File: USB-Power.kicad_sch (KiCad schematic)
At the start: 39 parts, among them J3 USB_C_Receptacle_USB2.0_16P, J4 USB_C_Receptacle_USB2.0_16P, SW3 SW_SPDT, U4 USBLC6-2SC6, U5 BQ24075RGT, U6 BQ27441DRZR-G1A, U7 TPS61023DRLT

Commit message: layouting component to PCB
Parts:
- C45, C47, C48, C49, C50, C51, C52, C53: footprint (none) -> Capacitor_SMD:C_0603_1608Metric
- C46, C54: footprint (none) -> Capacitor_SMD:C_0402_1005Metric
- D3, D4: footprint (none) -> LED_SMD:LED_0805_2012Metric
- J3, J4: footprint (none) -> Connector_USB:USB_C_Receptacle_G-Switch_GT-USB-7010ASV
- L3: footprint (none) -> Inductor_SMD:L_Abracon_ASPI-0425
- R11, R12, R13, R14, R15, R16, R17, R18, R19, R20, R21, R22, R23, R24, R25, R26, R27, R28, R29: footprint (none) -> Resistor_SMD:R_0402_1005Metric
- SW3: footprint (none) -> Button_Switch_SMD:SW_SPDT_CK_JS102011SAQN
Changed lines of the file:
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@@
 			)
 		)
-		(property "Footprint" ""
+		(property "Footprint" "Capacitor_SMD:C_0603_1608Metric"
 			(at 272.7452 34.29 0)
 			(effects
@@
 			)
 		)
-		(property "Footprint" ""
+		(property "Footprint" "Connector_USB:USB_C_Receptacle_G-Switch_GT-USB-7010ASV"
 			(at 34.29 104.14 0)
 			(effects
@@
 			)
 		)
-		(property "Footprint" ""
+		(property "Footprint" "Capacitor_SMD:C_0603_1608Metric"
 			(at 147.0152 184.15 0)
 			(effects
@@
 			)
 		)
-		(property "Footprint" ""
+		(property "Footprint" "Resistor_SMD:R_0402_1005Metric"
 			(at 191.262 60.96 90)
 			(effects
@@
 			)
 		)
-		(property "Footprint" ""
+		(property "Footprint" "LED_SMD:LED_0805_2012Metric"
 			(at 251.46 52.07 0)
 			(effects
@@
 			)
 		)
-		(property "Footprint" ""
+		(property "Footprint" "Resistor_SMD:R_0402_1005Metric"
 			(at 74.422 175.26 90)
 			(effects
@@
 			)
 		)
-		(property "Footprint" ""
+		(property "Footprint" "Resistor_SMD:R_0402_1005Metric"
 			(at 55.88 96.52 0)
 			(effects
@@
 			)
 		)
-		(property "Footprint" ""
+		(property "Footprint" "Button_Switch_SMD:SW_SPDT_CK_JS102011SAQN"
 			(at 157.48 34.29 0)
 			(effects
@@
 			)
 		)
-		(property "Footprint" ""
+		(property "Footprint" "Resistor_SMD:R_0402_1005Metric"
 			(at 55.88 30.48 0)
 			(effects
@@
 			)
 		)
-		(property "Footprint" ""
+		(property "Footprint" "Resistor_SMD:R_0402_1005Metric"
 			(at 209.55 128.27 0)
 			(effects
@@
 			)
 		)
-		(property "Footprint" ""
+		(property "Footprint" "Capacitor_SMD:C_0603_1608Metric"
 			(at 65.7352 184.15 0)
 			(effects
@@
 			)
 		)
-		(property "Footprint" ""
+		(property "Footprint" "Resistor_SMD:R_0402_1005Metric"
 			(at 180.34 39.37 0)
 			(effects
@@
 			)
 		)
-		(property "Footprint" ""
+		(property "Footprint" "Resistor_SMD:R_0402_1005Metric"
 			(at 74.422 160.02 90)
 			(effects
@@
 			)
 		)
-		(property "Footprint" ""
+		(property "Footprint" "LED_SMD:LED_0805_2012Metric"
 			(at 251.46 63.5 0)
 			(effects
@@
 			)
 		)
-		(property "Footprint" ""
+		(property "Footprint" "Resistor_SMD:R_0402_1005Metric"
 			(at 55.88 93.98 0)
 			(effects
@@
 			)
 		)
-		(property "Footprint" ""
+		(property "Footprint" "Resistor_SMD:R_0402_1005Metric"
 			(at 151.638 25.4 90)
 			(effects
@@
 			)
 		)
-		(property "Footprint" ""
+		(property "Footprint" "Capacitor_SMD:C_0402_1005Metric"
 			(at 38.1 180.34 0)
 			(effects
@@
 			)
 		)
-		(property "Footprint" ""
+		(property "Footprint" "Capacitor_SMD:C_0603_1608Metric"
 			(at 261.3152 34.29 0)
 			(effects
@@
 			)
 		)
-		(property "Footprint" ""
+		(property "Footprint" "Resistor_SMD:R_0402_1005Metric"
 			(at 266.7 144.78 0)
 			(effects
@@
 			)
 		)
-		(property "Footprint" ""
+		(property "Footprint" "Capacitor_SMD:C_0603_1608Metric"
 			(at 236.22 117.1448 0)
 			(effects
@@
 			)
 		)
-		(property "Footprint" ""
+		(property "Footprint" "Resistor_SMD:R_0402_1005Metric"
 			(at 235.712 36.83 90)
 			(effects
@@
 			)
 		)
-		(property "Footprint" ""
+		(property "Footprint" "Inductor_SMD:L_Abracon_ASPI-0425"
 			(at 93.98 175.26 0)
 			(effects
@@
 			)
 		)
-		(property "Footprint" ""
+		(property "Footprint" "Resistor_SMD:R_0402_1005Metric"
 			(at 209.042 147.32 90)
 			(effects
@@
 			)
 		)
-		(property "Footprint" ""
+		(property "Footprint" "Resistor_SMD:R_0402_1005Metric"
 			(at 173.482 60.96 90)
 			(effects
@@
 			)
 		)
-		(property "Footprint" ""
+		(property "Footprint" "Connector_USB:USB_C_Receptacle_G-Switch_GT-USB-7010ASV"
 			(at 34.29 40.64 0)
 			(effects
@@
 			)
 		)
-		(property "Footprint" ""
+		(property "Footprint" "Resistor_SMD:R_0402_1005Metric"
 			(at 182.372 60.96 90)
 			(effects
@@
 			)
 		)
-		(property "Footprint" ""
+		(property "Footprint" "Capacitor_SMD:C_0603_1608Metric"
 			(at 53.0352 184.15 0)
 			(effects
@@
 			)
 		)
-		(property "Footprint" ""
+		(property "Footprint" "Resistor_SMD:R_0402_1005Metric"
 			(at 55.88 33.02 0)
 			(effects
@@
 			)
 		)
-		(property "Footprint" ""
+		(property "Footprint" "Resistor_SMD:R_0402_1005Metric"
 			(at 92.202 160.02 90)
 			(effects
@@
 			)
 		)
-		(property "Footprint" ""
+		(property "Footprint" "Capacitor_SMD:C_0402_1005Metric"
 			(at 269.24 131.1148 0)
 			(effects
@@
 			)
 		)
-		(property "Footprint" ""
+		(property "Footprint" "Capacitor_SMD:C_0603_1608Metric"
 			(at 249.8852 34.29 0)
 			(effects
@@
 			)
 		)
-		(property "Footprint" ""
+		(property "Footprint" "Resistor_SMD:R_0402_1005Metric"
 			(at 212.09 128.27 0)
 			(effects
@@
 			)
 		)
-		(property "Footprint" ""
+		(property "Footprint" "Resistor_SMD:R_0402_1005Metric"
 			(at 240.03 52.07 0)
 			(effects
@@
 			)
 		)
-		(property "Footprint" ""
+		(property "Footprint" "Capacitor_SMD:C_0603_1608Metric"
 			(at 158.4452 184.15 0)
 			(effects
@@
 			)
 		)
-		(property "Footprint" ""
+		(property "Footprint" "Resistor_SMD:R_0402_1005Metric"
 			(at 240.03 63.5 0)
 			(effects

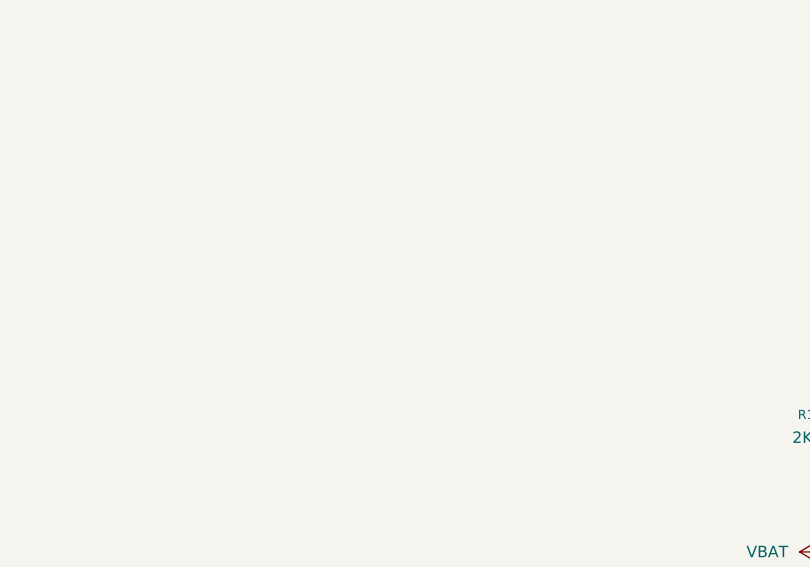
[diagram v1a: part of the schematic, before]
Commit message: Add connection from OSPI Flash and LCD to MCU
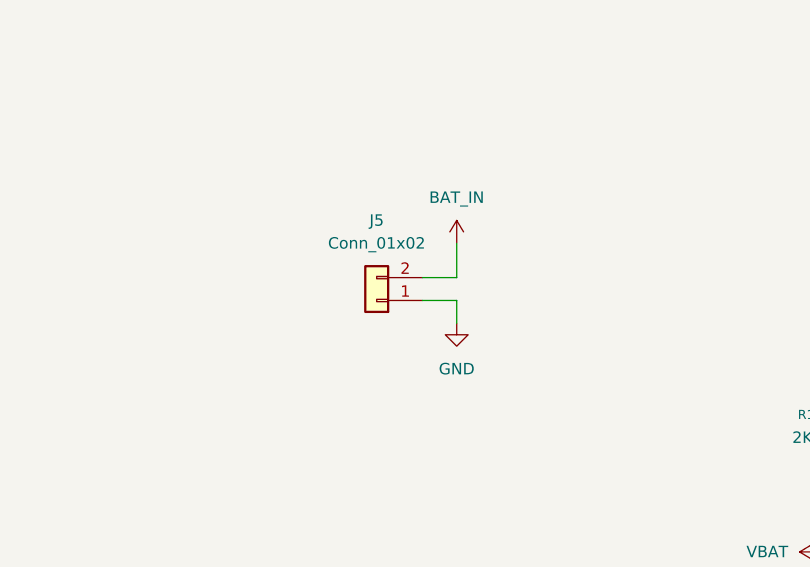
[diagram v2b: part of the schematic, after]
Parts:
- added J5: Conn_01x02, Connector_PinHeader_2.54mm:PinHeader_1x02_P2.54mm_Vertical, symbol Connector_Generic:Conn_01x02
- R15: footprint Resistor_SMD:R_0402_1005Metric -> Resistor_SMD:R_1206_3216Metric
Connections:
- net BAT_IN: now also J5.2 (Pin_2)
- net GND: now also J5.1 (Pin_1)
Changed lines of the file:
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@@
 	(wire
 		(pts
+			(xy 162.56 111.76) (xy 166.37 111.76)
+		)
+		(stroke
+			(width 0)
+			(type default)
+		)
+	)
+	(wire
+		(pts
 			(xy 45.72 40.64) (xy 46.99 40.64)
 		)
@@
 	(wire
 		(pts
+			(xy 162.56 114.3) (xy 166.37 114.3)
+		)
+		(stroke
+			(width 0)
+			(type default)
+		)
+	)
+	(wire
+		(pts
 			(xy 237.49 46.99) (xy 237.49 40.64)
 		)
@@
 	(wire
 		(pts
+			(xy 166.37 114.3) (xy 166.37 116.84)
+		)
+		(stroke
+			(width 0)
+			(type default)
+		)
+	)
+	(wire
+		(pts
 			(xy 224.79 129.54) (xy 227.33 129.54)
 		)
@@
 	(wire
 		(pts
+			(xy 166.37 111.76) (xy 166.37 107.95)
+		)
+		(stroke
+			(width 0)
+			(type default)
+		)
+	)
+	(wire
+		(pts
 			(xy 207.01 142.24) (xy 210.82 142.24)
 		)
@@
 			)
 		)
-		(property "Footprint" "Resistor_SMD:R_0402_1005Metric"
+		(property "Footprint" "Resistor_SMD:R_1206_3216Metric"
 			(at 209.042 147.32 90)
 			(effects
@@
 	)
 	(symbol
+		(lib_id "Connector_Generic:Conn_01x02")
+		(at 157.48 114.3 180)
+		(unit 1)
+		(exclude_from_sim no)
+		(in_bom yes)
+		(on_board yes)
+		(dnp no)
+		(fields_autoplaced yes)
+		(property "Reference" "J5"
+			(at 157.48 105.41 0)
+			(effects
+				(font
+					(size 1.27 1.27)
+				)
+			)
+		)
+		(property "Value" "Conn_01x02"
+			(at 157.48 107.95 0)
+			(effects
+				(font
+					(size 1.27 1.27)
+				)
+			)
+		)
+		(property "Footprint" "Connector_PinHeader_2.54mm:PinHeader_1x02_P2.54mm_Vertical"
+			(at 157.48 114.3 0)
+			(effects
+				(font
+					(size 1.27 1.27)
+				)
+				(hide yes)
+			)
+		)
+		(property "Datasheet" "~"
+			(at 157.48 114.3 0)
+			(effects
+				(font
+					(size 1.27 1.27)
+				)
+				(hide yes)
+			)
+		)
+		(property "Description" "Generic connector, single row, 01x02, script generated (kicad-library-utils/schlib/autogen/connector/)"
+			(at 157.48 114.3 0)
+			(effects
+				(font
+					(size 1.27 1.27)
+				)
+				(hide yes)
+			)
+		)
+		(pin "1"
+		)
+		(pin "2"
+		)
+		(instances
+			(project ""
+				(path "/439b205a-84a5-4f71-9e86-c11126d8e75a/29f38a54-1de1-4072-8da2-38b5cdc8846d"
+					(reference "J5")
+					(unit 1)
+				)
+			)
+		)
+	)
+	(symbol
 		(lib_id "Device:R")
 		(at 184.15 60.96 0)
@@
 	)
 	(symbol
+		(lib_id "power:GND")
+		(at 166.37 116.84 0)
+		(unit 1)
+		(exclude_from_sim no)
+		(in_bom yes)
+		(on_board yes)
+		(dnp no)
+		(fields_autoplaced yes)
+		(property "Reference" "#PWR0121"
+			(at 166.37 123.19 0)
+			(effects
+				(font
+					(size 1.27 1.27)
+				)
+				(hide yes)
+			)
+		)
+		(property "Value" "GND"
+			(at 166.37 121.92 0)
+			(effects
+				(font
+					(size 1.27 1.27)
+				)
+			)
+		)
+		(property "Footprint" ""
+			(at 166.37 116.84 0)
+			(effects
+				(font
+					(size 1.27 1.27)
+				)
+				(hide yes)
+			)
+		)
+		(property "Datasheet" ""
+			(at 166.37 116.84 0)
+			(effects
+				(font
+					(size 1.27 1.27)
+				)
+				(hide yes)
+			)
+		)
+		(property "Description" "Power symbol creates a global label with name \"GND\" , ground"
+			(at 166.37 116.84 0)
+			(effects
+				(font
+					(size 1.27 1.27)
+				)
+				(hide yes)
+			)
+		)
+		(pin "1"
+		)
+		(instances
+			(project "chroma-pixel-u5g9"
+				(path "/439b205a-84a5-4f71-9e86-c11126d8e75a/29f38a54-1de1-4072-8da2-38b5cdc8846d"
+					(reference "#PWR0121")
+					(unit 1)
+				)
+			)
+		)
+	)
+	(symbol
 		(lib_id "Device:R")
 		(at 93.98 160.02 0)
@@
 					(unit 1)
 				)
+			)
+		)
+	)
+	(symbol
+		(lib_id "power:VBUS")
+		(at 166.37 107.95 0)
+		(unit 1)
+		(exclude_from_sim no)
+		(in_bom yes)
+		(on_board yes)
+		(dnp no)
+		(fields_autoplaced yes)
+		(property "Reference" "#PWR092"
+			(at 166.37 111.76 0)
+			(effects
+				(font
+					(size 1.27 1.27)
+				)
+				(hide yes)
+			)
+		)
+		(property "Value" "BAT_IN"
+			(at 166.37 102.87 0)
+			(effects
+				(font
+					(size 1.27 1.27)
+				)
+			)
+		)
+		(property "Footprint" ""
+			(at 166.37 107.95 0)
+			(effects
+				(font
+					(size 1.27 1.27)
+				)
+				(hide yes)
+			)
+		)
+		(property "Datasheet" ""
+			(at 166.37 107.95 0)
+			(effects
+				(font
+					(size 1.27 1.27)
+				)
+				(hide yes)
+			)
+		)
+		(property "Description" "Power symbol creates a global label with name \"VBUS\""
+			(at 166.37 107.95 0)
+			(effects
+				(font
+					(size 1.27 1.27)
+				)
+				(hide yes)
+			)
+		)
+		(pin "1"
+		)
+		(instances
+			(project "chroma-pixel-u5g9"
+				(path "/439b205a-84a5-4f71-9e86-c11126d8e75a/29f38a54-1de1-4072-8da2-38b5cdc8846d"
+					(reference "#PWR092")
+					(unit 1)
+				)

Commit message: Change bypass capacitor to 0201
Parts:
- C54: footprint Capacitor_SMD:C_0402_1005Metric -> Capacitor_SMD:C_0201_0603Metric
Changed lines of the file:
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@@
 			)
 		)
-		(property "Footprint" "Capacitor_SMD:C_0402_1005Metric"
+		(property "Footprint" "Capacitor_SMD:C_0201_0603Metric"
 			(at 38.1 180.34 0)
 			(effects
